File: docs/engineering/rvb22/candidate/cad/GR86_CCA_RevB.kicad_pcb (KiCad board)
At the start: 4 copper layers, 88.3 x 61.3 mm, 199 parts, among them J201 TC2030-IDC-NL / UART, J202 RESET — short to reset, J203 BOOT — hold low on reset, J401 U.FL-R-SMT-1(80), Q101 STD25NF20 /200V, U101 LTC4367HMS8#WTRPBF, U121 LM5164DDAR, U151 LM63615DQPWPRQ1, U201 ESP32-S3-WROOM-1-N8R2, U202 TPS3808G33-Q1 3.07V RESET, U301 TCAN3403DRBRQ1, U401 PA1616D, U402 SN74LVC2G125DCUR, U403 MIC5504-3.3YM5-TR, U404 SN74LVC2G125DCUR, U501 TPS26600PWPR, U502 OPA2333AIDR

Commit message: RVB22 I13: trial denser ESP thermal vias and retain failed thermal evidence
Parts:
- U201: footprint RevB:ESP32-S3-WROOM-1_RVB22_U201 -> RevB:ESP32-S3-WROOM-1_RVB22_U201_TH48
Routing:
- net GND: vias 106 -> 154

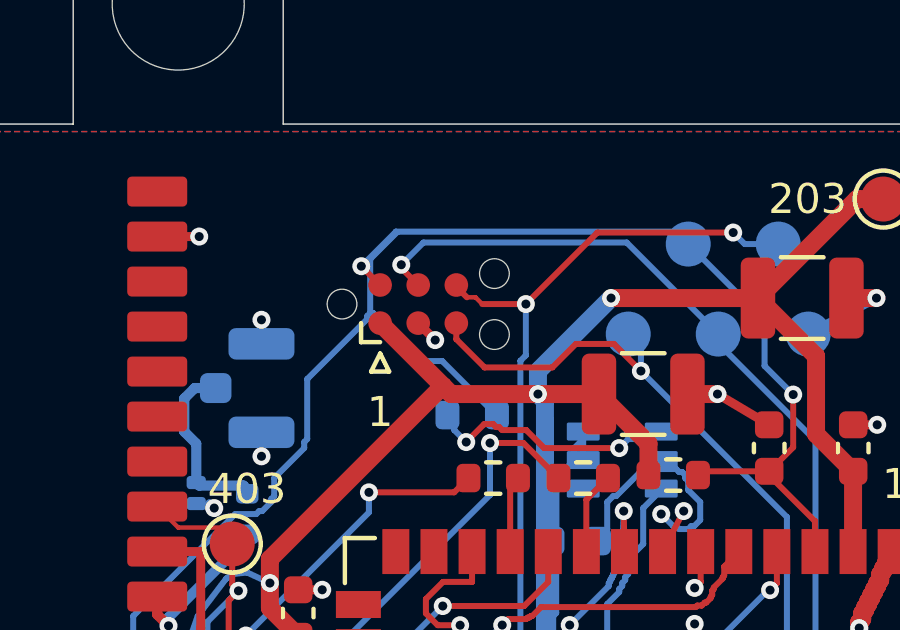
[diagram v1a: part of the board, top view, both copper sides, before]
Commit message: I14: correct Tag-Connect contact clearances and preserve I13 native evidence
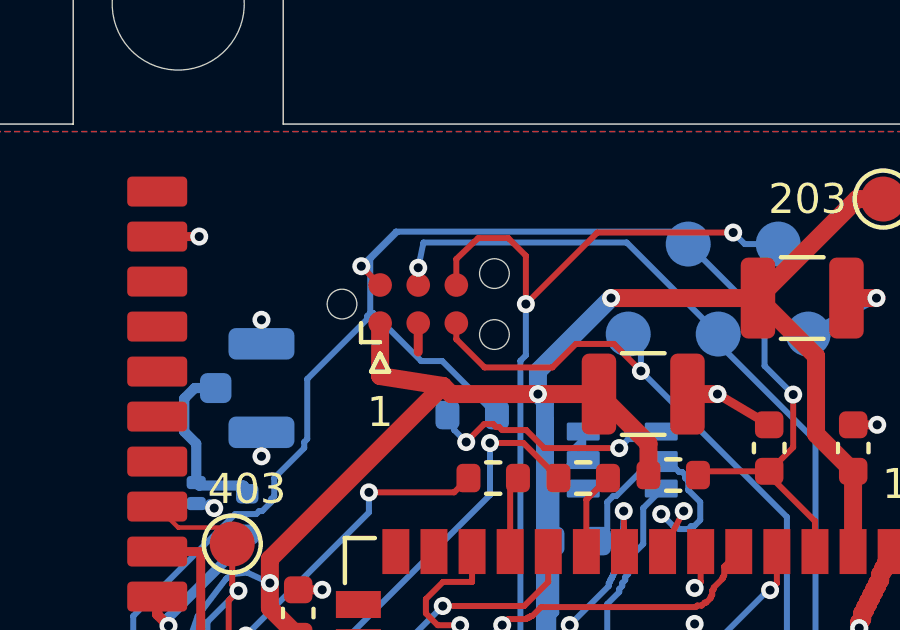
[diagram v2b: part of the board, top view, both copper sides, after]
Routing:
- net ESP_GPIO0: track 116.6 -> 119.3 mm
- net +3V3: track 347.2 -> 348.1 mm
- net UART0_RX: track 40.3 -> 39.7 mm
- net GND: track 176.6 -> 176.8 mm, vias 154 -> 153
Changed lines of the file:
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@@
 (segment (start 78.5 34) (end 78.5 34.8) (width 0.3) (locked yes) (layer "F.Cu") (net 1))
 (segment (start 84.2609 10.3359) (end 84.2609 7.7359) (width 0.6) (layer "F.Cu") (net 1))
-(segment (start 71.8243 8.7292) (end 69.73 6.635) (width 0.6) (layer "F.Cu") (net 1))
 (segment (start 77.025 9) (end 78.675 10.65) (width 0.6) (layer "F.Cu") (net 1))
 (via (at 79.8 25.5) (size 0.6) (drill 0.3) (layers "F.Cu" "B.Cu") (locked yes) (net 1))
@@
 (segment (start 40.3 21.5) (end 39.4 22.4) (width 0.2) (locked yes) (layer "In1.Cu") (net 27))
 (segment (start 41.7 22.1) (end 41 21.4) (width 0.2) (locked yes) (layer "In1.Cu") (net 27))
-(segment (start 73.1341 6) (end 72.9088 5.7747) (width 0.15) (layer "F.Cu") (net 28))
 (segment (start 68.9 30.9) (end 68.2 30.9) (width 0.2) (locked yes) (layer "F.Cu") (net 28))
 (segment (start 13.6 38.8) (end 13.5 38.7) (width 0.2) (locked yes) (layer "F.Cu") (net 28))
@@
 (segment (start 58.1 31.6) (end 58.1 31.7) (width 0.2) (locked yes) (layer "F.Cu") (net 28))
 (segment (start 25.5 39) (end 25.2 39.3) (width 0.2) (locked yes) (layer "F.Cu") (net 28))
-(segment (start 73.1341 6) (end 74.5887 6) (width 0.2) (layer "F.Cu") (net 28))
 (segment (start 66.2 26.1) (end 66 25.9) (width 0.2) (locked yes) (layer "F.Cu") (net 28))
 (segment (start 70.2548 31.75) (end 70.2548 30.7383) (width 0.2) (layer "F.Cu") (net 28))
@@
 (segment (start 25.8 37.4) (end 25.6 37.6) (width 0.2) (locked yes) (layer "F.Cu") (net 28))
 (segment (start 13.4 38.7) (end 13.3 38.6) (width 0.2) (locked yes) (layer "F.Cu") (net 28))
-(segment (start 72.6216 5.7747) (end 72.27 5.4231) (width 0.2) (layer "F.Cu") (net 28))
 (segment (start 13.8 38.9) (end 13.7 38.8) (width 0.2) (locked yes) (layer "F.Cu") (net 28))
 (segment (start 70.2548 31.75) (end 70.2548 34.0298) (width 0.2) (layer "F.Cu") (net 28))
@@
 (segment (start 25.2 39.3) (end 24.9 39.3) (width 0.2) (locked yes) (layer "F.Cu") (net 28))
 (segment (start 16 39.9) (end 15.9 39.8) (width 0.2) (locked yes) (layer "F.Cu") (net 28))
-(segment (start 72.9088 5.7747) (end 72.6216 5.7747) (width 0.15) (layer "F.Cu") (net 28))
 (segment (start 15.2 39.7) (end 15.1 39.6) (width 0.2) (locked yes) (layer "F.Cu") (net 28))
 (segment (start 16.5 40.1) (end 16.4 40) (width 0.2) (locked yes) (layer "F.Cu") (net 28))
@@
 (segment (start 15.9 39.8) (end 15.8 39.8) (width 0.2) (locked yes) (layer "F.Cu") (net 28))
 (segment (start 17.1 40.4) (end 17 40.3) (width 0.2) (locked yes) (layer "F.Cu") (net 28))
-(segment (start 72.27 5.4231) (end 72.27 5.365) (width 0.2) (layer "F.Cu") (net 28))
 (segment (start 46.3 29.7) (end 46.2 29.6) (width 0.2) (locked yes) (layer "F.Cu") (net 28))
 (segment (start 24.9 39.3) (end 24.8 39.4) (width 0.2) (locked yes) (layer "F.Cu") (net 28))
@@
 (segment (start 43 5.525) (end 43 6.525) (width 0.3) (layer "F.Cu") (net 30))
 (segment (start 67 15.525) (end 67.8 15.525) (width 0.3) (layer "F.Cu") (net 30))
-(segment (start 71 6.635) (end 71.5657 7.2007) (width 0.3) (layer "F.Cu") (net 30))
 (segment (start 82.7 10.025) (end 80.975 9) (width 0.3) (layer "F.Cu") (net 30))
 (segment (start 84 39.1) (end 84 40.4) (width 0.3) (locked yes) (layer "F.Cu") (net 30))
@@
 (via (at 35.9 40.5) (size 0.6) (drill 0.3) (layers "F.Cu" "B.Cu") (net 30))
 (via (at 18.775 13.7) (size 0.6) (drill 0.3) (layers "F.Cu" "B.Cu") (net 30))
-(via (at 71.5657 7.2007) (size 0.6) (drill 0.3) (layers "F.Cu" "B.Cu") (net 30))
 (via (at 24.45 29.5) (size 0.6) (drill 0.3) (layers "F.Cu" "B.Cu") (net 30))
 (via (at 24.275 8.865) (size 0.6) (drill 0.3) (layers "F.Cu" "B.Cu") (net 30))
@@
 (segment (start 84.1157 24.8242) (end 84.2423 24.8242) (width 0.2) (layer "F.Cu") (net 86))
 (segment (start 82.203 30.2201) (end 82.203 26.7369) (width 0.2) (layer "F.Cu") (net 86))
-(segment (start 71 5.365) (end 70.4351 4.8001) (width 0.2) (layer "F.Cu") (net 86))
 (segment (start 82.203 26.7369) (end 84.1157 24.8242) (width 0.2) (layer "F.Cu") (net 86))
-(segment (start 70.4351 4.8001) (end 70.4351 4.6893) (width 0.2) (layer "F.Cu") (net 86))
 (segment (start 81.6848 30.7383) (end 82.203 30.2201) (width 0.2) (layer "F.Cu") (net 86))
 (segment (start 81.6848 31.75) (end 81.6848 30.7383) (width 0.2) (layer "F.Cu") (net 86))
-(via (at 70.4351 4.6893) (size 0.6) (drill 0.3) (layers "F.Cu" "B.Cu") (net 86))
+(via (at 71 4.79) (size 0.6) (drill 0.3) (layers "F.Cu" "B.Cu") (net 86))
 (via (at 84.2423 24.8242) (size 0.6) (drill 0.3) (layers "F.Cu" "B.Cu") (net 86))
 (segment (start 81 7.3126) (end 84.2423 10.5549) (width 0.2) (layer "B.Cu") (net 86))
 (segment (start 81 7) (end 81 7.3126) (width 0.2) (layer "B.Cu") (net 86))
-(segment (start 70.4351 4.6893) (end 71.1758 3.9486) (width 0.2) (layer "B.Cu") (net 86))
+(segment (start 71 4.79) (end 71.1758 3.9486) (width 0.2) (layer "B.Cu") (net 86))
 (segment (start 77.9486 3.9486) (end 81 7) (width 0.2) (layer "B.Cu") (net 86))
 (segment (start 71.1758 3.9486) (end 77.9486 3.9486) (width 0.2) (layer "B.Cu") (net 86))
@@
 (via (at 79.269766 23.075) (size 0.6) (drill 0.2) (layers "F.Cu" "B.Cu") (net 30))
 (via (at 79.719766 23.075) (size 0.6) (drill 0.2) (layers "F.Cu" "B.Cu") (net 30))
+(segment (start 69.73 6.635) (end 69.73 8.4) (width 0.6) (layer "F.Cu") (net 1))
+(segment (start 69.73 8.4) (end 71.8243 8.7292) (width 0.6) (layer "F.Cu") (net 1))
+(segment (start 71 6.635) (end 71 7.6) (width 0.3) (layer "F.Cu") (net 30))
+(segment (start 71 5.365) (end 71 4.79) (width 0.2) (layer "F.Cu") (net 86))
+(segment (start 72.27 5.365) (end 72.27 4.5) (width 0.2) (layer "F.Cu") (net 28))
+(segment (start 72.27 4.5) (end 73 3.8) (width 0.2) (layer "F.Cu") (net 28))
+(segment (start 73 3.8) (end 74 3.8) (width 0.2) (layer "F.Cu") (net 28))
+(segment (start 74 3.8) (end 74.5887 4.3887) (width 0.2) (layer "F.Cu") (net 28))
+(segment (start 74.5887 4.3887) (end 74.5887 6) (width 0.2) (layer "F.Cu") (net 28))
 )

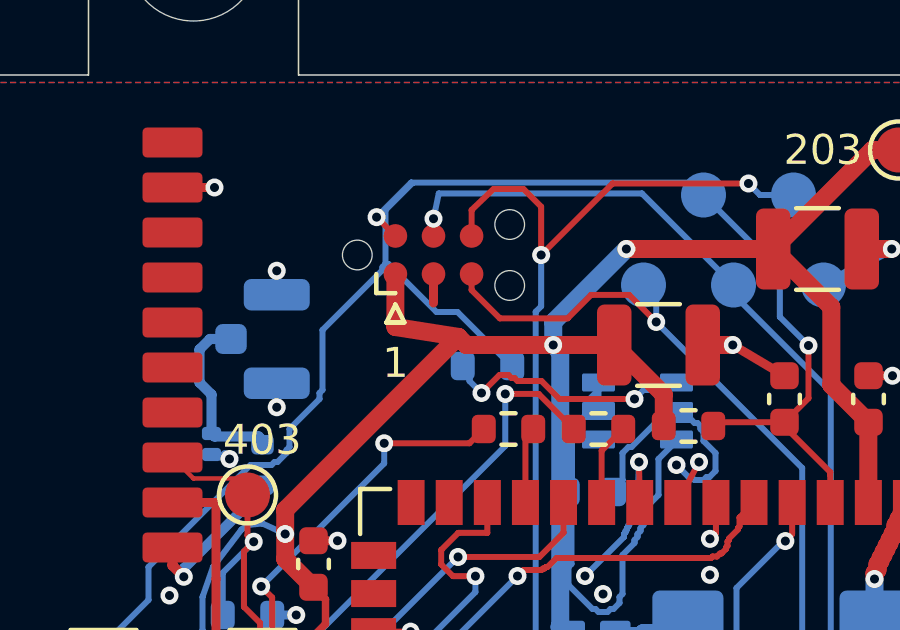
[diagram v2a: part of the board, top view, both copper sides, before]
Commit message: RVB22 I15: restore service ground stitch clear of programming contacts
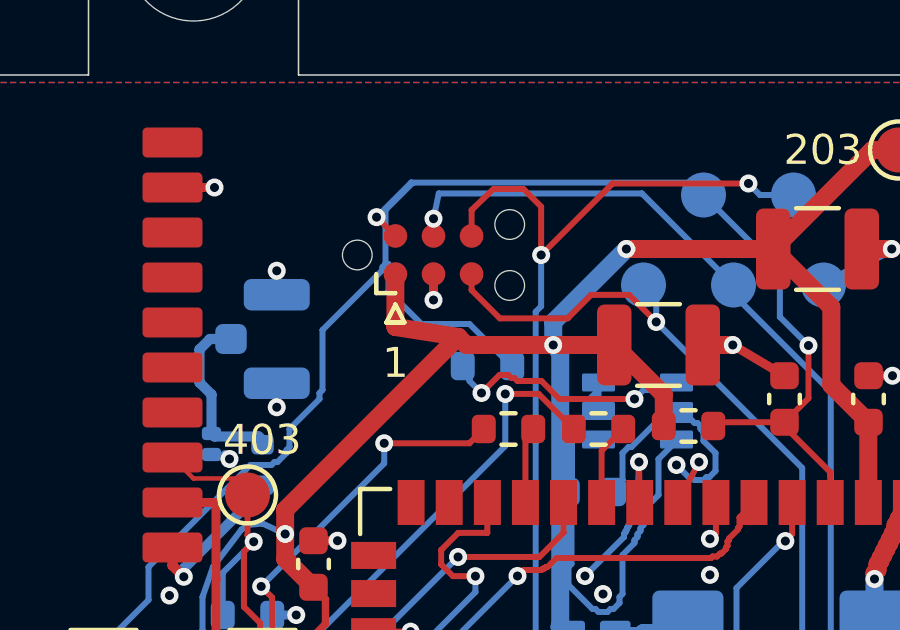
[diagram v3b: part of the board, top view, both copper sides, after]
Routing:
- net ESP_EN: track 129.8 -> 130.3 mm
- net GND: vias 153 -> 154
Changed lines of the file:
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@@
 (footprint "RevB:C_0603_1608Metric_RVB22_C205" (layer "B.Cu") (at 76.2 13.9 0) (attr smd) (property "Reference" "C205" (at 0 -1.7 0) (layer "B.Fab") (effects (font (size 0.7 0.7) (thickness 0.1)) (justify mirror))) (property "Value" "100n /50V X7R" (at 0 0 0) (layer "B.Fab") (hide yes) (effects (font (size 0.7 0.7) (thickness 0.1)) (justify mirror))) (property "MPN" "GCM188R71H104KA57D" (at 0 0 0) (layer "B.Fab") (hide yes) (effects (font (size 0.7 0.7) (thickness 0.1)) (justify mirror))) (property "Manufacturer" "Murata" (at 0 0 0) (layer "B.Fab") (hide yes) (effects (font (size 0.7 0.7) (thickness 0.1)) (justify mirror))) (property "Datasheet" "https://www.murata.com/en-us/products/productdetail?partno=GCM188R71H104KA57D" (at 0 0 0) (layer "B.Fab") (hide yes) (effects (font (size 0.7 0.7) (thickness 0.1)) (justify mirror))) (property "LCSC" "C85864" (at 0 0 0) (layer "B.Fab") (hide yes) (effects (font (size 0.7 0.7) (thickness 0.1)) (justify mirror))) (property "Assembly" "FACTORY" (at 0 0 0) (layer "B.Fab") (hide yes) (effects (font (size 0.7 0.7) (thickness 0.1)) (justify mirror))) (property "Description" "RVB21 staged reset correction; native validation pending" (at 0 0 0) (layer "B.Fab") (hide yes) (effects (font (size 0.7 0.7) (thickness 0.1)) (justify mirror))) (pad "1" smd roundrect (at -0.775 0 0) (size 0.9 0.95) (layers "B.Cu" "B.Paste" "B.Mask") (roundrect_rratio 0.25) (net 1 "+3V3")) (pad "2" smd roundrect (at 0.775 0 0) (size 0.9 0.95) (layers "B.Cu" "B.Paste" "B.Mask") (roundrect_rratio 0.25) (net 30 "GND")) (fp_rect (start -1.505 -0.755) (end 1.505 0.755) (stroke (width 0.05) (type solid)) (fill none) (layer "B.CrtYd")) (fp_rect (start -0.8 -0.4) (end 0.8 0.4) (stroke (width 0.1) (type solid)) (fill none) (layer "B.Fab")) (model "${KIPRJMOD}/models/ENVELOPE_C_0603_1608Metric_RVB22_C205.step" (offset (xyz 0 0 0)) (scale (xyz 1 1 1)) (rotate (xyz 0 0 0))))
 (segment (start 73.625 9.7) (end 73.6 9.7) (width 0.2) (layer "B.Cu") (net 27))
-(segment (start 73.6 9.7) (end 71.8 7.9) (width 0.2) (layer "B.Cu") (net 27))
-(segment (start 71.8 7.9) (end 71.1 7.9) (width 0.2) (layer "B.Cu") (net 27))
-(segment (start 71.1 7.9) (end 69.5 6.3) (width 0.2) (layer "B.Cu") (net 27))
 (segment (start 69.5 6.3) (end 69.4 6.3) (width 0.2) (layer "B.Cu") (net 27))
 (segment (start 79.1 10.25) (end 79.1 10.2) (width 0.2) (layer "B.Cu") (net 129))
@@
 (segment (start 74 3.8) (end 74.5887 4.3887) (width 0.2) (layer "F.Cu") (net 28))
 (segment (start 74.5887 4.3887) (end 74.5887 6) (width 0.2) (layer "F.Cu") (net 28))
+(segment (start 69.5 6.3) (end 69.5 7.2) (width 0.2) (layer "B.Cu") (net 27))
+(segment (start 69.5 7.2) (end 70.6 8.3) (width 0.2) (layer "B.Cu") (net 27))
+(segment (start 70.6 8.3) (end 72.2 8.3) (width 0.2) (layer "B.Cu") (net 27))
+(segment (start 72.2 8.3) (end 73.6 9.7) (width 0.2) (layer "B.Cu") (net 27))
+(via (at 71 7.5) (size 0.6) (drill 0.3) (layers "F.Cu" "B.Cu") (net 30))
 )

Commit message: Correct GPS ground reference and UART power-plane underlap (I16)
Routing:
- net +3V3: track 348.1 -> 338.4 mm
